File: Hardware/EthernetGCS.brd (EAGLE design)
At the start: 73.7 x 42.2 mm, 67 parts, among them IC3 24AA00OT, IC4 PIC24FJ64GA002_QFN, J2 HR911105A, Q2 25Mhz, U1 MIC5219-3.3V, U3 MIC5219-3.3V, U4 ENC28J60-QFN, U5 MIC5219-3.3V, U7 FT232RL-BASICSSOP, X2 USB-A-H

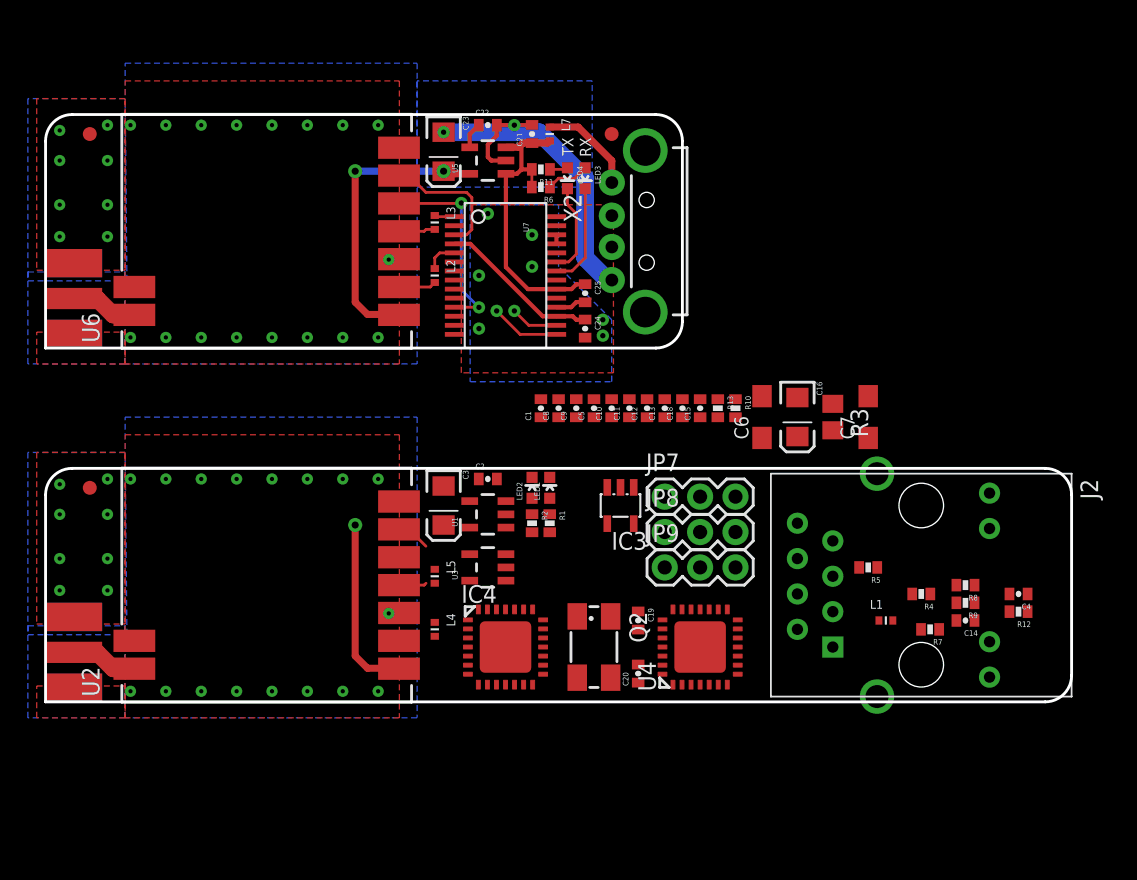
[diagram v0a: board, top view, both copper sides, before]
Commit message: Adding GPS port, RC output pull-ups. Connecting stuff, and changing parts positions.
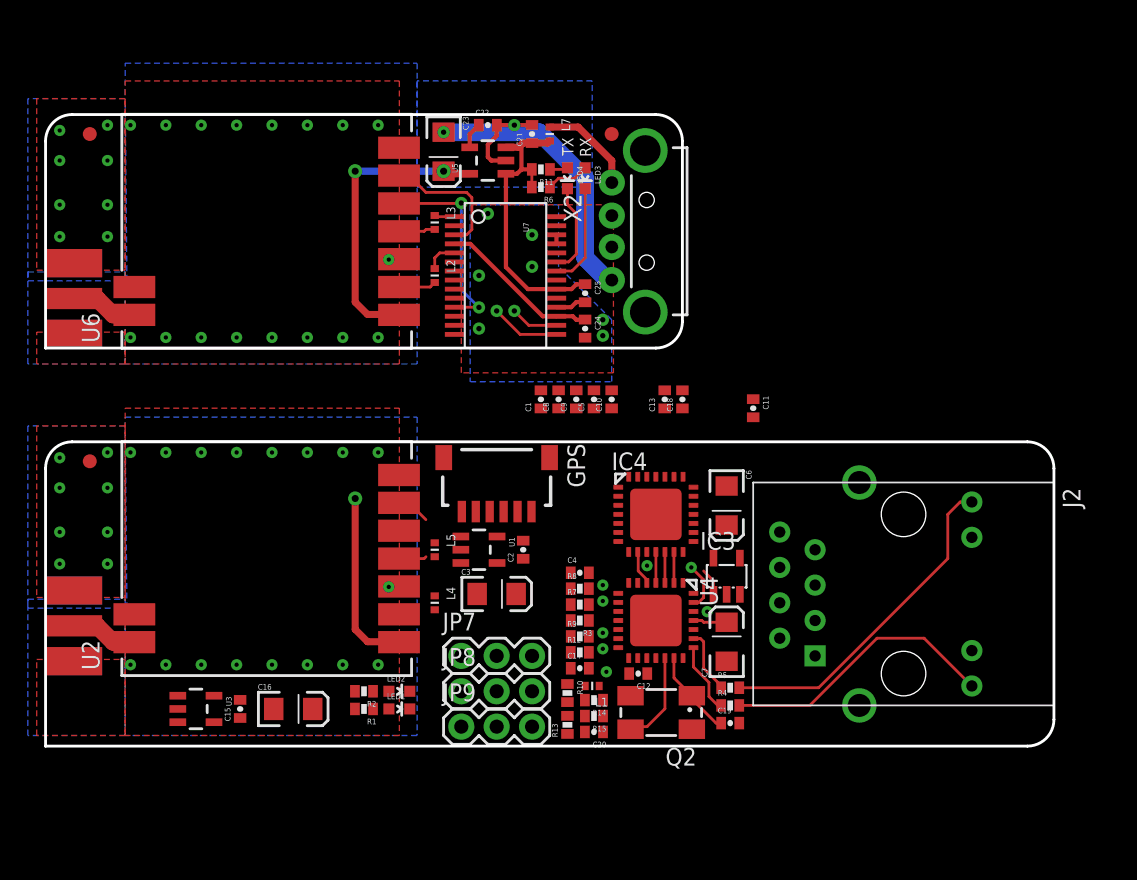
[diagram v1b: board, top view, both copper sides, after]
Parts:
- added GPS: SM06B-SRSS-TB, con-jst2:SM06B-SRSS-TB
- added R14, R15: (no value), SparkFun:0402-RES
- C6, C7: device rcl:SMC_A -> SparkFun:EIA3216
- R3: device rcl:R0805 -> SparkFun:0402-RES
- moved C16 41.8 mm to (17.8, 0.00), turned to 0 degrees
- moved C15 39.5 mm to (14.0, 0.00)
- moved R12 31.6 mm to (38.4, 4.06), turned to 0 degrees
- moved C4 31.5 mm to (38.4, 9.78), turned to 0 degrees
- moved C14 27.9 mm to (38.4, 2.92), turned to 0 degrees
- moved R9 27.8 mm to (38.4, 5.21), turned to 0 degrees
- moved R8 27.7 mm to (38.4, 8.64), turned to 0 degrees
- moved R7 25.2 mm to (38.4, 7.49), turned to 0 degrees
- moved R13 25.2 mm to (37.5, -1.14), turned to 90 degrees
- moved R10 23.7 mm to (37.5, 1.14)
- moved R3 23.3 mm to (38.4, 6.35), turned to 180 degrees
- moved U3 23.3 mm to (10.8, 0.00), turned to 270 degrees
- moved L1 21.6 mm to (39.2, 1.65), turned to 180 degrees
- moved LED1 19.2 mm to (25.4, 0.00), turned to 270 degrees
- moved C7 19.1 mm to (48.9, 4.83)
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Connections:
- new net CKLOUT: IC4.6, U4.27
- new net PD2: GPS.3
- new net PD3: GPS.4
- new net VCC: GPS.5
- net 3.3V: no longer C3.A, IC4.10, U1.5
- net ETH-CLK: now also IC4.11
- net ETH-CS: now also IC4.9
- net ETH-MISO: now also IC4.13
- net ETH-MOSI: now also IC4.12
- net GND: now also C6.C, C7.C, GPS.2, GPS.6, R3.2; no longer C6.-, C7.-, R3.1
- net LED_LINK: now also R4.2; no longer R5.2
- net LED_STATUS: now also R5.2; no longer R4.2
- net N$13: now also C7.A; no longer C6.+
- net N$17: now also R3.1; no longer R3.2
- net N$5: now also C6.A; no longer C7.+
- net RC1: now also R14.2
- net RC2: now also R15.2
- net SCL: now also IC4.14
- net SDA: now also IC4.15
- net V+: now also C3.A, IC4.10, U1.5
- net V_BAT: now also R14.1, R15.1
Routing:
- net CCT: track 0.00 -> 26.3 mm, vias 0 -> 1
- net LED_STATUS: track 0.00 -> 24.1 mm
- net LED_LINK: track 0.00 -> 20.1 mm
- net RD+: track 0.00 -> 15.9 mm, vias 0 -> 1
- net TD+: track 0.00 -> 15.3 mm, vias 0 -> 1
- net RD-: track 0.00 -> 13.5 mm, vias 0 -> 1
- net TD-: track 0.00 -> 12.7 mm, vias 0 -> 1
- net N$15: track 0.00 -> 6.71 mm
- net N$14: track 0.00 -> 6.39 mm
- net N$19: track 0.00 -> 5.11 mm
- net N$18: track 0.00 -> 4.61 mm
- net CKLOUT: track 0.00 -> 3.40 mm, vias 0 -> 1
- net ETH-CS: track 0.00 -> 2.81 mm
- net N$13: track 0.00 -> 2.43 mm
- net ETH-MOSI: track 0.00 -> 2.22 mm
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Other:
- board size 73.7 x 42.2 mm -> 72.4 x 45.3 mm

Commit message: Layout: tracing tracks.
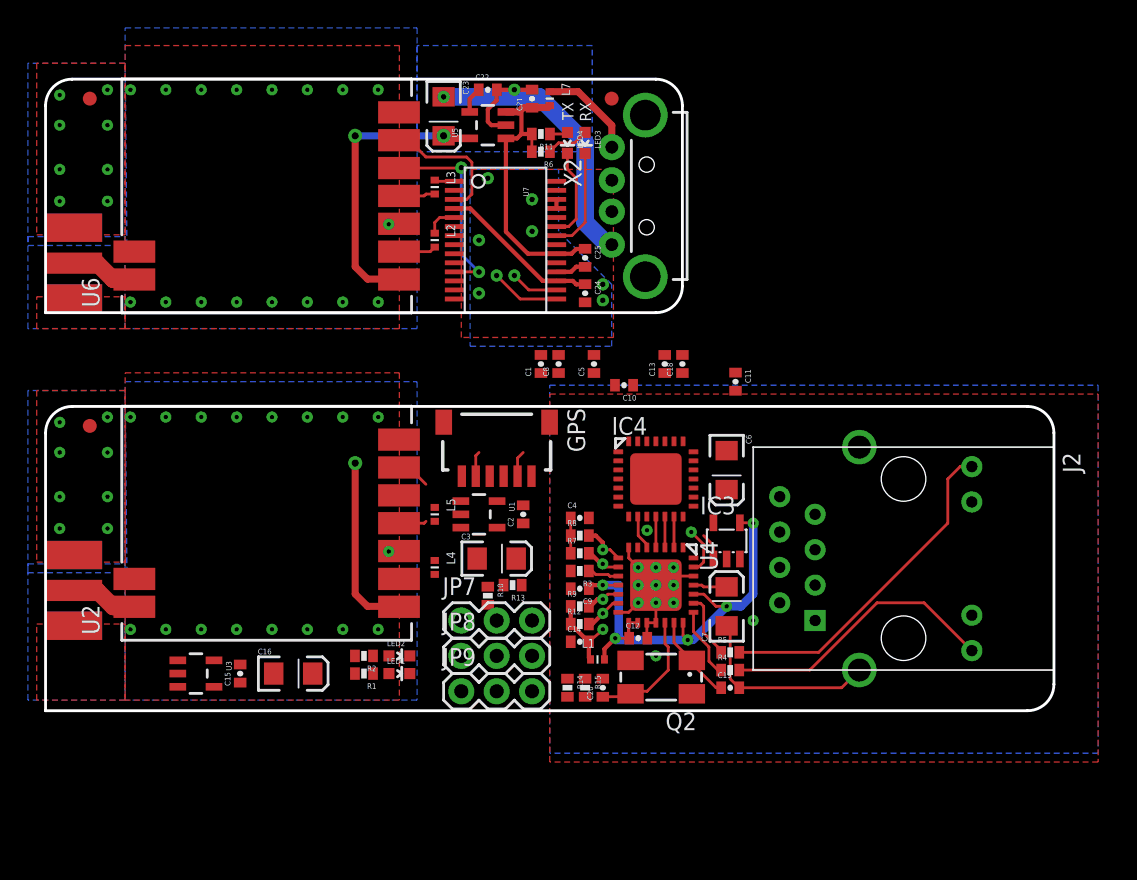
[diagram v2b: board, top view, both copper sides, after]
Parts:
- moved C9 13.6 mm to (38.4, 8.64), turned to 180 degrees
- moved R13 10.8 mm to (33.5, 8.89), turned to 180 degrees
- moved R10 9.03 mm to (31.8, 8.13)
- moved C4 3.94 mm to (38.4, 13.7)
- moved R8 3.81 mm to (38.4, 12.4)
- moved R7 3.68 mm to (38.4, 11.2)
- moved R3 3.56 mm to (38.4, 9.91)
- moved C20 3.24 mm to (40.0, 1.52), turned to 90 degrees
- moved C22 2.54 mm to (31.8, 44.5)
- moved L3 2.54 mm to (27.9, 37.5)
- moved L2 2.54 mm to (27.9, 33.7)
- moved U7 2.54 mm to (33.0, 33.7)
- moved C2 2.54 mm to (34.3, 14.0)
- moved IC4 2.54 mm to (43.8, 16.5)
- moved L5 2.54 mm to (27.9, 14.0)
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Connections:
- removed net VCC: GPS.5
- net V+: now also GPS.5
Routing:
- net V+: track 0.00 -> 36.6 mm, vias 1 -> 6
- net GND: track 29.9 -> 59.7 mm, vias 60 -> 70
- net CCT: track 26.3 -> 33.6 mm
- net TD-: track 12.7 -> 18.0 mm
- net TD+: track 15.3 -> 19.4 mm
- net RD+: track 15.9 -> 19.6 mm
- net RD-: track 13.5 -> 16.3 mm
- net N$17: track 0.00 -> 2.56 mm
- net N$22: track 0.00 -> 2.54 mm
- net N$15: track 6.71 -> 8.98 mm

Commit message: Continuing the board layout, adding connections to the schematic
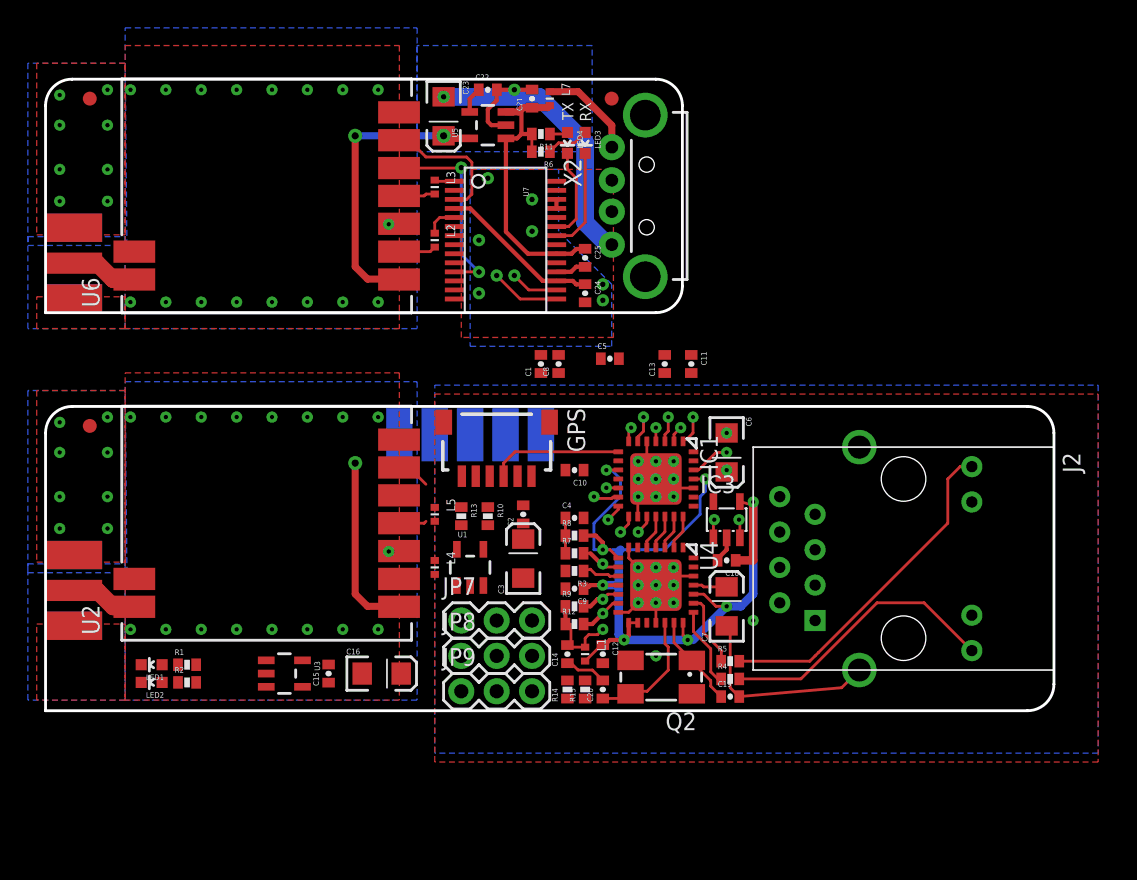
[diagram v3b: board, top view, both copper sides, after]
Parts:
- added U$10, U$11, U$12, U$7, U$9: SOLDER_PAD150_75, DIYdrones2:SOLD_PAD_150_75
- moved LED2 17.9 mm to (7.62, 1.91), turned to 90 degrees
- moved LED1 17.8 mm to (7.62, 3.17), turned to 90 degrees
- moved C18 14.5 mm to (48.9, 10.7), turned to 180 degrees
- moved R2 12.8 mm to (10.2, 1.91), turned to 0 degrees
- moved R1 12.7 mm to (10.2, 3.17), turned to 0 degrees
- moved C10 7.06 mm to (38.0, 17.1)
- moved C15 6.35 mm to (20.3, 2.54)
- moved U3 6.35 mm to (17.1, 2.54)
- moved C16 6.35 mm to (24.1, 2.54)
- moved R13 6.17 mm to (29.8, 13.8), turned to 270 degrees
- moved R10 5.71 mm to (31.8, 13.8)
- moved U1 3.86 mm to (30.5, 10.2), turned to 0 degrees
- moved C11 3.42 mm to (46.4, 24.8)
- moved C12 2.79 mm to (40.0, 3.94), turned to 270 degrees
- moved C3 1.91 mm to (34.3, 10.8), turned to 90 degrees
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- renumbered IC4 to IC1
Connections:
- removed net ETH-MISO: IC1.13, U4.2
- removed net ETH-MOSI: IC1.12, U4.3
- removed net PD2: GPS.3
- removed net PD3: GPS.4
- removed net VSS: IC1.5
- new net !MCLR: IC1.26, U$12.P$1
- new net ETH-SI: IC1.20, U4.3
- new net ETH-SO: IC1.21, U4.2
- new net GPS1: GPS.3, IC1.8
- new net GPS2: GPS.4, IC1.11
- new net PGC: IC1.2, U$7.P$1
- new net PGD: IC1.1, U$9.P$1
- net 3.3V: no longer IC1.25
- net 5V: no longer R1.2, R2.2
- net CKLOUT: no longer IC1.6
- net ETH-CLK: now also IC1.19; no longer IC1.11
- net ETH-CS: now also IC1.18; no longer IC1.9
- net GND: now also IC1.5, LED1.C, LED2.C, U$10.P$1
- net LED_RX: now also IC1.6, R1.2; no longer LED1.C
- net LED_TX: now also IC1.7, R2.2; no longer LED2.C
- net RC1: now also IC1.12
- net RC2: now also IC1.13
- net RX: now also IC1.4
- net TX: now also IC1.3
- net V+: now also IC1.25, U$11.P$1
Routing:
- net V+: track 36.6 -> 65.6 mm, vias 6 -> 7
- net SDA: track 0.00 -> 12.7 mm, vias 0 -> 2
- net N$5: track 0.00 -> 10.4 mm, vias 0 -> 2
- net GPS1: track 0.00 -> 9.50 mm
- net SCL: track 1.97 -> 10.5 mm, vias 0 -> 2
- net GND: track 59.7 -> 67.3 mm, vias 70 -> 80
- net CKLOUT: track 3.40 -> 0.00 mm, vias 1 -> 0
- net !MCLR: track 0.00 -> 2.90 mm, vias 0 -> 1
- net ETH-SO: track 0.00 -> 2.49 mm
- net ETH-SI: track 0.00 -> 2.49 mm
- net ETH-MOSI: track 2.22 -> 0.00 mm
- net ETH-MISO: track 2.22 -> 0.00 mm
- net PGD: track 0.00 -> 2.19 mm, vias 0 -> 1
- net LED_RX: track 0.00 -> 1.92 mm, vias 0 -> 1
- net TX: track 0.00 -> 1.84 mm, vias 0 -> 1
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
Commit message: More Layout, and designing the power section of the board
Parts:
- added D1: MBR120VLSFT1G, adafruit:SOD-123
- added D4: MMSZ5233BT1G, adafruit:SOD-123
- added F2: 500mA, SparkFun:PTC-1206
- added JP1: (no value), SparkFun-Connectors:1X03
- added SJ1: (no value), SparkFun:SJ_2
- moved C1 34.2 mm to (10.9, 1.02), turned to 0 degrees
- moved JP7 15.7 mm to (33.7, -8.89)
- moved C11 14.0 mm to (32.4, 24.8)
- moved C5 13.5 mm to (33.0, 14.0), turned to 90 degrees
- moved C16 7.01 mm to (17.1, 3.17)
- moved C15 6.16 mm to (14.4, 1.02), turned to 180 degrees
- moved U3 5.12 mm to (12.1, 3.17)
- moved R10 3.81 mm to (35.6, 13.8)
- moved C2 3.18 mm to (31.1, 14.0)
- moved C13 2.29 mm to (42.5, 26.0)
- moved LED1 1.91 mm to (5.71, 3.17)
- moved LED2 1.91 mm to (5.71, 1.91)
- moved C10 1.90 mm to (38.0, 15.2)
- moved R1 1.90 mm to (8.26, 3.17)
- moved R2 1.90 mm to (8.26, 1.91)
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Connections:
- removed net BAT_SEN1: JP7.3, R10.1
- removed net V_BAT: JP7.2, JP8.2, JP9.2, R14.1, R15.1
- new net N$10: JP7.3, SJ1.3
- new net N$11: JP1.2, R10.1
- new net N$6: D1.C, F2.1
- new net V_IN: D1.A, SJ1.2
- new net V_RC: JP7.2, JP8.2, JP9.2, R14.1, R15.1, SJ1.1
- net 5V: now also D4.C, F2.2
- net BAT_SEN: now also IC1.22
- net CTS: now also IC1.9
- net GND: now also D4.A, JP1.1
- net RTS: now also IC1.28
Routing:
- net !MCLR: track 2.90 -> 24.8 mm
- net RTS: track 2.43 -> 23.6 mm, vias 0 -> 1
- net PGC: track 1.18 -> 19.0 mm
- net TX: track 1.84 -> 19.6 mm
- net RC1: track 0.86 -> 18.2 mm
- net RC2: track 1.84 -> 18.3 mm
- net RX: track 0.98 -> 16.7 mm
- net LED_RX: track 1.92 -> 16.5 mm
- net PGD: track 2.19 -> 16.2 mm
- net BAT_SEN: track 0.00 -> 14.0 mm, vias 0 -> 1
- net LED_TX: track 1.05 -> 14.8 mm
- net 3.3V: track 34.2 -> 21.3 mm, vias 3 -> 2

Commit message: More Layout...
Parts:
- moved LED2 38.6 mm to (40.0, 19.7), turned to 0 degrees
- moved LED1 36.4 mm to (38.1, 19.7), turned to 0 degrees
- moved R1 32.8 mm to (38.0, 17.0), turned to 180 degrees
- moved R2 32.7 mm to (38.0, 15.6), turned to 180 degrees
- moved C5 29.8 mm to (6.35, 0.64), turned to 180 degrees
- moved SJ1 15.9 mm to (27.3, 6.35), flipped to the bottom, turned to 270 degrees
- moved JP1 15.4 mm to (34.9, 8.89), turned to 180 degrees
- moved JP7 14.7 mm to (34.9, 5.71), turned to 180 degrees
- moved R15 12.1 mm to (26.7, 0.64), turned to 0 degrees
- moved R14 10.9 mm to (26.7, 3.17), turned to 0 degrees
- moved F2 7.41 mm to (18.4, 1.91), turned to 90 degrees
- moved D1 7.24 mm to (22.2, 0.64)
- moved L4 6.99 mm to (21.0, 10.2)
- moved R10 6.54 mm to (29.6, 11.2), turned to 180 degrees
- moved L5 5.71 mm to (22.2, 14.0)
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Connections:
- net 5V: now also GPS.5
- net V+: no longer GPS.5
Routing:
- net V+: track 65.6 -> 90.2 mm, vias 7 -> 8
- net V_RC: track 0.00 -> 21.6 mm
- net 5V: track 22.5 -> 42.7 mm, vias 0 -> 1
- net BAT_SEN: track 14.0 -> 26.5 mm, vias 1 -> 2
- net RC2: track 18.3 -> 26.8 mm
- net RC1: track 18.2 -> 26.0 mm
- net N$11: track 0.00 -> 3.17 mm
- net GND: track 67.3 -> 64.2 mm, vias 80 -> 81
- net N$7: track 1.99 -> 0.00 mm
- net N$2: track 0.00 -> 1.63 mm
- net RTS: track 23.6 -> 22.0 mm
- net SCL: track 10.5 -> 11.6 mm
- net SDA: track 12.7 -> 13.7 mm
- net RD+: track 20.0 -> 20.7 mm
- net PGD: track 16.2 -> 15.6 mm
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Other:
- board size 72.4 x 45.3 mm -> 72.4 x 46 mm
